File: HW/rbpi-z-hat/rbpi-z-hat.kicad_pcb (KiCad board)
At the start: 4 copper layers, 65 x 30 mm, 98 parts, among them IC1 BQ24315DSGR, J1 RBPI_CONN, J10 JST_GH, J11 Conn_01x10, J12 Conn_01x06, J13 Conn_01x10, J14 Conn_01x06, J15 Conn_01x06, J16 Conn_01x10, J8 Conn_01x06_MountingPin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

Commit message: Replaced LSM9DS1 with BMI160/QMI8658C
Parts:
- removed C23: 4.7uF/10V, Capacitor_SMD:C_0805_2012Metric
- removed C24, C25, C27: 0.1uF, Capacitor_SMD:C_0603_1608Metric
- removed C26: 10nF/16V, Capacitor_SMD:C_0603_1608Metric
- removed U8: LSM9DS1, Package_LGA:LGA-24L_3x3.5mm_P0.43mm
- added C16: 0.1uF, Capacitor_SMD:C_0603_1608Metric, F.Cu at (88.3, 65.7)
- added C35: 0.1uF, Capacitor_SMD:C_0603_1608Metric, F.Cu at (88.3, 68.2)
- added U10: BMI160, Package_LGA:Bosch_LGA-14_3x2.5mm_P0.5mm, F.Cu at (92.7, 66.6)
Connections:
- net /LSM_nCS renamed /BMI_nCS

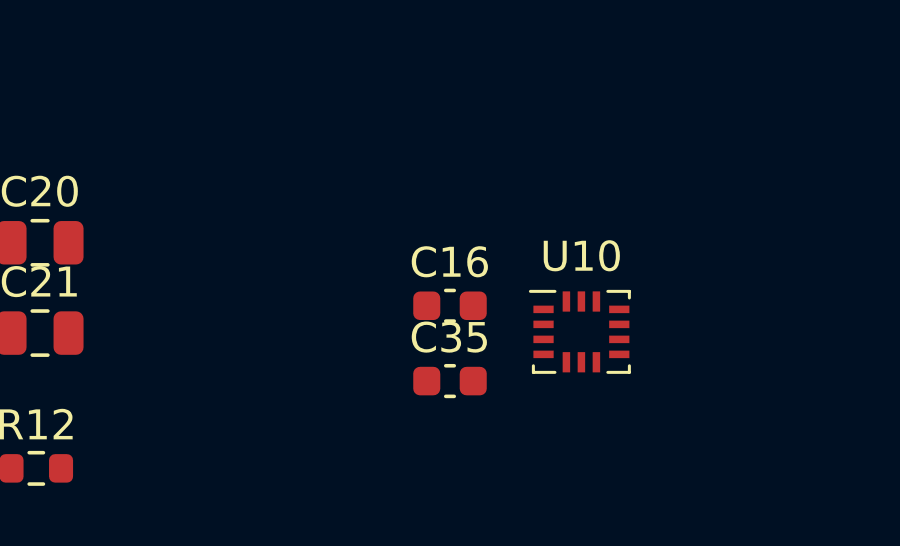
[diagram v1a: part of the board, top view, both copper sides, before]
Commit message: Changed capasitors to 0402
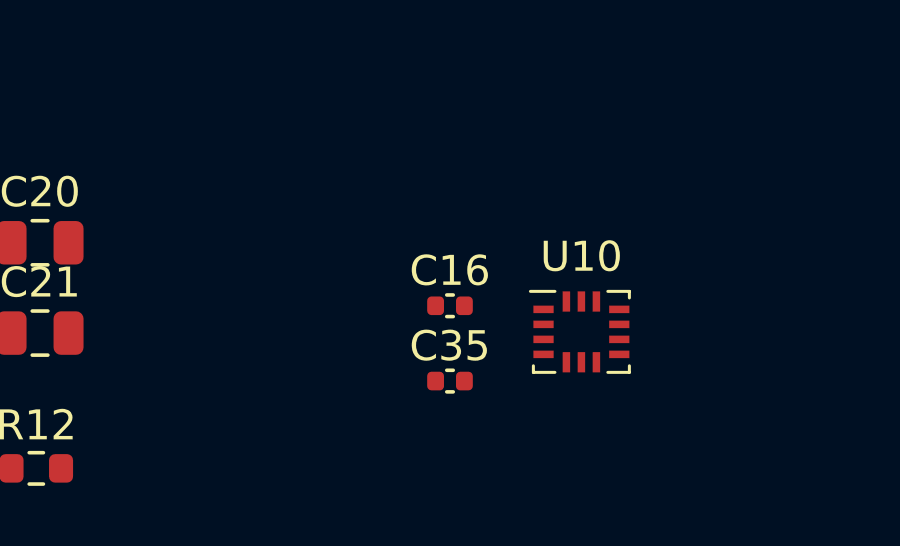
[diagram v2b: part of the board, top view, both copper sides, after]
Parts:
- C16, C35: footprint Capacitor_SMD:C_0603_1608Metric -> Capacitor_SMD:C_0402_1005Metric
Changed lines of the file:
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@@
     )
   )
-  (footprint "Capacitor_SMD:C_0603_1608Metric" (layer "F.Cu")
+  (footprint "Capacitor_SMD:C_0402_1005Metric" (layer "F.Cu")
     (at 88.275 68.21)
-    (descr "Capacitor SMD 0603 (1608 Metric), square (rectangular) end terminal, IPC_7351 nominal, (Body size source: IPC-SM-782 page 76, https://www.pcb-3d.com/wordpress/wp-content/uploads/ipc-sm-782a_amendment_1_and_2.pdf), generated with kicad-footprint-generator")
+    (descr "Capacitor SMD 0402 (1005 Metric), square (rectangular) end terminal, IPC_7351 nominal, (Body size source: IPC-SM-782 page 76, https://www.pcb-3d.com/wordpress/wp-content/uploads/ipc-sm-782a_amendment_1_and_2.pdf), generated with kicad-footprint-generator")
     (tags "capacitor")
     (property "Sheetfile" "BMI160_QMI8658C.kicad_sch")
@@
     (property "ki_keywords" "cap capacitor")
     (attr smd)
-    (fp_text reference "C35" (at 0 -1.43) (layer "F.SilkS")
-        (effects (font (size 1 1) (thickness 0.15)))
-    )
-    (fp_text value "0.1uF" (at 0 1.43) (layer "F.Fab")
+    (fp_text reference "C35" (at 0 -1.16) (layer "F.SilkS")
+        (effects (font (size 1 1) (thickness 0.15)))
+    )
+    (fp_text value "0.1uF" (at 0 1.16) (layer "F.Fab")
         (effects (font (size 1 1) (thickness 0.15)))
     )
     (fp_text user "${REFERENCE}" (at 0 0) (layer "F.Fab")
-        (effects (font (size 0.4 0.4) (thickness 0.06)))
-    )
-    (fp_line (start -0.14058 -0.51) (end 0.14058 -0.51)
-      (stroke (width 0.12) (type solid)) (layer "F.SilkS"))
-    (fp_line (start -0.14058 0.51) (end 0.14058 0.51)
-      (stroke (width 0.12) (type solid)) (layer "F.SilkS"))
-    (fp_line (start -1.48 -0.73) (end 1.48 -0.73)
-      (stroke (width 0.05) (type solid)) (layer "F.CrtYd"))
-    (fp_line (start -1.48 0.73) (end -1.48 -0.73)
-      (stroke (width 0.05) (type solid)) (layer "F.CrtYd"))
-    (fp_line (start 1.48 -0.73) (end 1.48 0.73)
-      (stroke (width 0.05) (type solid)) (layer "F.CrtYd"))
-    (fp_line (start 1.48 0.73) (end -1.48 0.73)
-      (stroke (width 0.05) (type solid)) (layer "F.CrtYd"))
-    (fp_line (start -0.8 -0.4) (end 0.8 -0.4)
-      (stroke (width 0.1) (type solid)) (layer "F.Fab"))
-    (fp_line (start -0.8 0.4) (end -0.8 -0.4)
-      (stroke (width 0.1) (type solid)) (layer "F.Fab"))
-    (fp_line (start 0.8 -0.4) (end 0.8 0.4)
-      (stroke (width 0.1) (type solid)) (layer "F.Fab"))
-    (fp_line (start 0.8 0.4) (end -0.8 0.4)
-      (stroke (width 0.1) (type solid)) (layer "F.Fab"))
-    (pad "1" smd roundrect (at -0.775 0) (size 0.9 0.95) (layers "F.Cu" "F.Paste" "F.Mask") (roundrect_rratio 0.25)
+        (effects (font (size 0.25 0.25) (thickness 0.04)))
+    )
+    (fp_line (start -0.107836 -0.36) (end 0.107836 -0.36)
+      (stroke (width 0.12) (type solid)) (layer "F.SilkS"))
+    (fp_line (start -0.107836 0.36) (end 0.107836 0.36)
+      (stroke (width 0.12) (type solid)) (layer "F.SilkS"))
+    (fp_line (start -0.91 -0.46) (end 0.91 -0.46)
+      (stroke (width 0.05) (type solid)) (layer "F.CrtYd"))
+    (fp_line (start -0.91 0.46) (end -0.91 -0.46)
+      (stroke (width 0.05) (type solid)) (layer "F.CrtYd"))
+    (fp_line (start 0.91 -0.46) (end 0.91 0.46)
+      (stroke (width 0.05) (type solid)) (layer "F.CrtYd"))
+    (fp_line (start 0.91 0.46) (end -0.91 0.46)
+      (stroke (width 0.05) (type solid)) (layer "F.CrtYd"))
+    (fp_line (start -0.5 -0.25) (end 0.5 -0.25)
+      (stroke (width 0.1) (type solid)) (layer "F.Fab"))
+    (fp_line (start -0.5 0.25) (end -0.5 -0.25)
+      (stroke (width 0.1) (type solid)) (layer "F.Fab"))
+    (fp_line (start 0.5 -0.25) (end 0.5 0.25)
+      (stroke (width 0.1) (type solid)) (layer "F.Fab"))
+    (fp_line (start 0.5 0.25) (end -0.5 0.25)
+      (stroke (width 0.1) (type solid)) (layer "F.Fab"))
+    (pad "1" smd roundrect (at -0.48 0) (size 0.56 0.62) (layers "F.Cu" "F.Paste" "F.Mask") (roundrect_rratio 0.25)
       (net 44 "/SENS_VDD") (pintype "passive"))
-    (pad "2" smd roundrect (at 0.775 0) (size 0.9 0.95) (layers "F.Cu" "F.Paste" "F.Mask") (roundrect_rratio 0.25)
+    (pad "2" smd roundrect (at 0.48 0) (size 0.56 0.62) (layers "F.Cu" "F.Paste" "F.Mask") (roundrect_rratio 0.25)
       (net 45 "/SENS_FGND") (pintype "passive"))
-    (model "${KICAD6_3DMODEL_DIR}/Capacitor_SMD.3dshapes/C_0603_1608Metric.wrl"
+    (model "${KICAD6_3DMODEL_DIR}/Capacitor_SMD.3dshapes/C_0402_1005Metric.wrl"
       (offset (xyz 0 0 0))
       (scale (xyz 1 1 1))
@@
       ))
   )
-  (footprint "Capacitor_SMD:C_0603_1608Metric" (layer "F.Cu")
+  (footprint "Capacitor_SMD:C_0402_1005Metric" (layer "F.Cu")
     (at 88.275 65.7)
-    (descr "Capacitor SMD 0603 (1608 Metric), square (rectangular) end terminal, IPC_7351 nominal, (Body size source: IPC-SM-782 page 76, https://www.pcb-3d.com/wordpress/wp-content/uploads/ipc-sm-782a_amendment_1_and_2.pdf), generated with kicad-footprint-generator")
+    (descr "Capacitor SMD 0402 (1005 Metric), square (rectangular) end terminal, IPC_7351 nominal, (Body size source: IPC-SM-782 page 76, https://www.pcb-3d.com/wordpress/wp-content/uploads/ipc-sm-782a_amendment_1_and_2.pdf), generated with kicad-footprint-generator")
     (tags "capacitor")
     (property "Sheetfile" "BMI160_QMI8658C.kicad_sch")
@@
     (property "ki_keywords" "cap capacitor")
     (attr smd)
-    (fp_text reference "C16" (at 0 -1.43) (layer "F.SilkS")
-        (effects (font (size 1 1) (thickness 0.15)))
-    )
-    (fp_text value "0.1uF" (at 0 1.43) (layer "F.Fab")
+    (fp_text reference "C16" (at 0 -1.16) (layer "F.SilkS")
+        (effects (font (size 1 1) (thickness 0.15)))
+    )
+    (fp_text value "0.1uF" (at 0 1.16) (layer "F.Fab")
         (effects (font (size 1 1) (thickness 0.15)))
     )
     (fp_text user "${REFERENCE}" (at 0 0) (layer "F.Fab")
-        (effects (font (size 0.4 0.4) (thickness 0.06)))
-    )
-    (fp_line (start -0.14058 -0.51) (end 0.14058 -0.51)
-      (stroke (width 0.12) (type solid)) (layer "F.SilkS"))
-    (fp_line (start -0.14058 0.51) (end 0.14058 0.51)
-      (stroke (width 0.12) (type solid)) (layer "F.SilkS"))
-    (fp_line (start -1.48 -0.73) (end 1.48 -0.73)
-      (stroke (width 0.05) (type solid)) (layer "F.CrtYd"))
-    (fp_line (start -1.48 0.73) (end -1.48 -0.73)
-      (stroke (width 0.05) (type solid)) (layer "F.CrtYd"))
-    (fp_line (start 1.48 -0.73) (end 1.48 0.73)
-      (stroke (width 0.05) (type solid)) (layer "F.CrtYd"))
-    (fp_line (start 1.48 0.73) (end -1.48 0.73)
-      (stroke (width 0.05) (type solid)) (layer "F.CrtYd"))
-    (fp_line (start -0.8 -0.4) (end 0.8 -0.4)
-      (stroke (width 0.1) (type solid)) (layer "F.Fab"))
-    (fp_line (start -0.8 0.4) (end -0.8 -0.4)
-      (stroke (width 0.1) (type solid)) (layer "F.Fab"))
-    (fp_line (start 0.8 -0.4) (end 0.8 0.4)
-      (stroke (width 0.1) (type solid)) (layer "F.Fab"))
-    (fp_line (start 0.8 0.4) (end -0.8 0.4)
-      (stroke (width 0.1) (type solid)) (layer "F.Fab"))
-    (pad "1" smd roundrect (at -0.775 0) (size 0.9 0.95) (layers "F.Cu" "F.Paste" "F.Mask") (roundrect_rratio 0.25)
+        (effects (font (size 0.25 0.25) (thickness 0.04)))
+    )
+    (fp_line (start -0.107836 -0.36) (end 0.107836 -0.36)
+      (stroke (width 0.12) (type solid)) (layer "F.SilkS"))
+    (fp_line (start -0.107836 0.36) (end 0.107836 0.36)
+      (stroke (width 0.12) (type solid)) (layer "F.SilkS"))
+    (fp_line (start -0.91 -0.46) (end 0.91 -0.46)
+      (stroke (width 0.05) (type solid)) (layer "F.CrtYd"))
+    (fp_line (start -0.91 0.46) (end -0.91 -0.46)
+      (stroke (width 0.05) (type solid)) (layer "F.CrtYd"))
+    (fp_line (start 0.91 -0.46) (end 0.91 0.46)
+      (stroke (width 0.05) (type solid)) (layer "F.CrtYd"))
+    (fp_line (start 0.91 0.46) (end -0.91 0.46)
+      (stroke (width 0.05) (type solid)) (layer "F.CrtYd"))
+    (fp_line (start -0.5 -0.25) (end 0.5 -0.25)
+      (stroke (width 0.1) (type solid)) (layer "F.Fab"))
+    (fp_line (start -0.5 0.25) (end -0.5 -0.25)
+      (stroke (width 0.1) (type solid)) (layer "F.Fab"))
+    (fp_line (start 0.5 -0.25) (end 0.5 0.25)
+      (stroke (width 0.1) (type solid)) (layer "F.Fab"))
+    (fp_line (start 0.5 0.25) (end -0.5 0.25)
+      (stroke (width 0.1) (type solid)) (layer "F.Fab"))
+    (pad "1" smd roundrect (at -0.48 0) (size 0.56 0.62) (layers "F.Cu" "F.Paste" "F.Mask") (roundrect_rratio 0.25)
       (net 44 "/SENS_VDD") (pintype "passive"))
-    (pad "2" smd roundrect (at 0.775 0) (size 0.9 0.95) (layers "F.Cu" "F.Paste" "F.Mask") (roundrect_rratio 0.25)
+    (pad "2" smd roundrect (at 0.48 0) (size 0.56 0.62) (layers "F.Cu" "F.Paste" "F.Mask") (roundrect_rratio 0.25)
       (net 45 "/SENS_FGND") (pintype "passive"))
-    (model "${KICAD6_3DMODEL_DIR}/Capacitor_SMD.3dshapes/C_0603_1608Metric.wrl"
-      (offset (xyz 0 0 0))
-      (scale (xyz 1 1 1))
+    (model "${KICAD6_3DMODEL_DIR}/Capacitor_SMD.3dshapes/C_0402_1005Metric.wrl"
+      (offset (xyz 0 0 0))
+      (scale (xyz 1 1 1))

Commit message: Changes in PCB
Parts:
- moved C15 7.25 mm to (94.9, 40.1)
- moved C35 7.23 mm to (95.5, 68.0), turned to -90 degrees
- moved C14 6.72 mm to (96.7, 42.9), turned to 90 degrees
- moved C16 5.44 mm to (92.6, 69.0)
- moved C10 4.80 mm to (86.9, 48.8), turned to 90 degrees
- moved C13 1.15 mm to (90.6, 42.5), turned to 180 degrees
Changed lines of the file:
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@@
   )
   (footprint "Capacitor_SMD:C_0402_1005Metric" (layer "F.Cu")
-    (at 90.01 43.48)
+    (at 96.7 42.9 90)
     (descr "Capacitor SMD 0402 (1005 Metric), square (rectangular) end terminal, IPC_7351 nominal, (Body size source: IPC-SM-782 page 76, https://www.pcb-3d.com/wordpress/wp-content/uploads/ipc-sm-782a_amendment_1_and_2.pdf), generated with kicad-footprint-generator")
     (tags "capacitor")
@@
     (property "ki_keywords" "cap capacitor")
     (attr smd)
-    (fp_text reference "C14" (at 0 -1.16) (layer "F.SilkS")
-        (effects (font (size 1 1) (thickness 0.15)))
-    )
-    (fp_text value "4.7uF" (at 0 1.16) (layer "F.Fab")
-        (effects (font (size 1 1) (thickness 0.15)))
-    )
-    (fp_text user "${REFERENCE}" (at 0 0) (layer "F.Fab")
+    (fp_text reference "C14" (at 0 1.3 90) (layer "F.SilkS")
+        (effects (font (size 1 1) (thickness 0.15)))
+    )
+    (fp_text value "4.7uF" (at 0 1.16 90) (layer "F.Fab")
+        (effects (font (size 1 1) (thickness 0.15)))
+    )
+    (fp_text user "${REFERENCE}" (at 0 0 90) (layer "F.Fab")
         (effects (font (size 0.25 0.25) (thickness 0.04)))
     )
@@
     (fp_line (start 0.5 0.25) (end -0.5 0.25)
       (stroke (width 0.1) (type solid)) (layer "F.Fab"))
-    (pad "1" smd roundrect (at -0.48 0) (size 0.56 0.62) (layers "F.Cu" "F.Paste" "F.Mask") (roundrect_rratio 0.25)
+    (pad "1" smd roundrect (at -0.48 0 90) (size 0.56 0.62) (layers "F.Cu" "F.Paste" "F.Mask") (roundrect_rratio 0.25)
       (net 132 "Net-(U6-CAP)") (pintype "passive"))
-    (pad "2" smd roundrect (at 0.48 0) (size 0.56 0.62) (layers "F.Cu" "F.Paste" "F.Mask") (roundrect_rratio 0.25)
+    (pad "2" smd roundrect (at 0.48 0 90) (size 0.56 0.62) (layers "F.Cu" "F.Paste" "F.Mask") (roundrect_rratio 0.25)
       (net 45 "/SENS_FGND") (pintype "passive"))
     (model "${KICAD6_3DMODEL_DIR}/Capacitor_SMD.3dshapes/C_0402_1005Metric.wrl"
@@
   )
   (footprint "Capacitor_SMD:C_0402_1005Metric" (layer "F.Cu")
-    (at 90.01 41.51)
+    (at 90.6 42.5 180)
     (descr "Capacitor SMD 0402 (1005 Metric), square (rectangular) end terminal, IPC_7351 nominal, (Body size source: IPC-SM-782 page 76, https://www.pcb-3d.com/wordpress/wp-content/uploads/ipc-sm-782a_amendment_1_and_2.pdf), generated with kicad-footprint-generator")
     (tags "capacitor")
@@
     (fp_line (start 0.5 0.25) (end -0.5 0.25)
       (stroke (width 0.1) (type solid)) (layer "F.Fab"))
-    (pad "1" smd roundrect (at -0.48 0) (size 0.56 0.62) (layers "F.Cu" "F.Paste" "F.Mask") (roundrect_rratio 0.25)
+    (pad "1" smd roundrect (at -0.48 0 180) (size 0.56 0.62) (layers "F.Cu" "F.Paste" "F.Mask") (roundrect_rratio 0.25)
       (net 44 "/SENS_VDD") (pintype "passive"))
-    (pad "2" smd roundrect (at 0.48 0) (size 0.56 0.62) (layers "F.Cu" "F.Paste" "F.Mask") (roundrect_rratio 0.25)
+    (pad "2" smd roundrect (at 0.48 0 180) (size 0.56 0.62) (layers "F.Cu" "F.Paste" "F.Mask") (roundrect_rratio 0.25)
       (net 131 "Net-(C13-Pad2)") (pintype "passive"))
     (model "${KICAD6_3DMODEL_DIR}/Capacitor_SMD.3dshapes/C_0402_1005Metric.wrl"
@@
   )
   (footprint "Capacitor_SMD:C_0402_1005Metric" (layer "F.Cu")
-    (at 90.01 45.45)
+    (at 94.9 40.1)
     (descr "Capacitor SMD 0402 (1005 Metric), square (rectangular) end terminal, IPC_7351 nominal, (Body size source: IPC-SM-782 page 76, https://www.pcb-3d.com/wordpress/wp-content/uploads/ipc-sm-782a_amendment_1_and_2.pdf), generated with kicad-footprint-generator")
     (tags "capacitor")
@@
     (property "ki_keywords" "cap capacitor")
     (attr smd)
-    (fp_text reference "C15" (at 0 -1.16) (layer "F.SilkS")
+    (fp_text reference "C15" (at 2.4 0) (layer "F.SilkS")
         (effects (font (size 1 1) (thickness 0.15)))
     )
@@
   )
   (footprint "Capacitor_SMD:C_0402_1005Metric" (layer "F.Cu")
-    (at 88.275 68.21)
+    (at 95.5 68 -90)
     (descr "Capacitor SMD 0402 (1005 Metric), square (rectangular) end terminal, IPC_7351 nominal, (Body size source: IPC-SM-782 page 76, https://www.pcb-3d.com/wordpress/wp-content/uploads/ipc-sm-782a_amendment_1_and_2.pdf), generated with kicad-footprint-generator")
     (tags "capacitor")
@@
     (property "ki_keywords" "cap capacitor")
     (attr smd)
-    (fp_text reference "C35" (at 0 -1.16) (layer "F.SilkS")
-        (effects (font (size 1 1) (thickness 0.15)))
-    )
-    (fp_text value "0.1uF" (at 0 1.16) (layer "F.Fab")
-        (effects (font (size 1 1) (thickness 0.15)))
-    )
-    (fp_text user "${REFERENCE}" (at 0 0) (layer "F.Fab")
+    (fp_text reference "C35" (at 0 -1.16 90) (layer "F.SilkS")
+        (effects (font (size 1 1) (thickness 0.15)))
+    )
+    (fp_text value "0.1uF" (at 0 1.16 90) (layer "F.Fab")
+        (effects (font (size 1 1) (thickness 0.15)))
+    )
+    (fp_text user "${REFERENCE}" (at 0 0 90) (layer "F.Fab")
         (effects (font (size 0.25 0.25) (thickness 0.04)))
     )
@@
     (fp_line (start 0.5 0.25) (end -0.5 0.25)
       (stroke (width 0.1) (type solid)) (layer "F.Fab"))
-    (pad "1" smd roundrect (at -0.48 0) (size 0.56 0.62) (layers "F.Cu" "F.Paste" "F.Mask") (roundrect_rratio 0.25)
+    (pad "1" smd roundrect (at -0.48 0 270) (size 0.56 0.62) (layers "F.Cu" "F.Paste" "F.Mask") (roundrect_rratio 0.25)
       (net 44 "/SENS_VDD") (pintype "passive"))
-    (pad "2" smd roundrect (at 0.48 0) (size 0.56 0.62) (layers "F.Cu" "F.Paste" "F.Mask") (roundrect_rratio 0.25)
+    (pad "2" smd roundrect (at 0.48 0 270) (size 0.56 0.62) (layers "F.Cu" "F.Paste" "F.Mask") (roundrect_rratio 0.25)
       (net 45 "/SENS_FGND") (pintype "passive"))
     (model "${KICAD6_3DMODEL_DIR}/Capacitor_SMD.3dshapes/C_0402_1005Metric.wrl"
@@
     (property "ki_keywords" "I2C magnetic 3-axis sensor")
     (attr smd)
-    (fp_text reference "U6" (at 0 -2.7) (layer "F.SilkS")
+    (fp_text reference "U6" (at -1.02 -2.6) (layer "F.SilkS")
         (effects (font (size 1 1) (thickness 0.15)))
     )
@@
   )
   (footprint "Capacitor_SMD:C_0402_1005Metric" (layer "F.Cu")
-    (at 83.46 45.45)
+    (at 86.9 48.8 90)
     (descr "Capacitor SMD 0402 (1005 Metric), square (rectangular) end terminal, IPC_7351 nominal, (Body size source: IPC-SM-782 page 76, https://www.pcb-3d.com/wordpress/wp-content/uploads/ipc-sm-782a_amendment_1_and_2.pdf), generated with kicad-footprint-generator")
     (tags "capacitor")
@@
     (property "ki_keywords" "cap capacitor")
     (attr smd)
-    (fp_text reference "C10" (at 0 -1.16) (layer "F.SilkS")
-        (effects (font (size 1 1) (thickness 0.15)))
-    )
-    (fp_text value "4.7uF" (at 0 1.16) (layer "F.Fab")
-        (effects (font (size 1 1) (thickness 0.15)))
-    )
-    (fp_text user "${REFERENCE}" (at 0 0) (layer "F.Fab")
+    (fp_text reference "C10" (at 0 1.2 90) (layer "F.SilkS")
+        (effects (font (size 1 1) (thickness 0.15)))
+    )
+    (fp_text value "4.7uF" (at 0 1.16 90) (layer "F.Fab")
+        (effects (font (size 1 1) (thickness 0.15)))
+    )
+    (fp_text user "${REFERENCE}" (at 0 0 90) (layer "F.Fab")
         (effects (font (size 0.25 0.25) (thickness 0.04)))
     )
@@
     (fp_line (start 0.5 0.25) (end -0.5 0.25)
       (stroke (width 0.1) (type solid)) (layer "F.Fab"))
-    (pad "1" smd roundrect (at -0.48 0) (size 0.56 0.62) (layers "F.Cu" "F.Paste" "F.Mask") (roundrect_rratio 0.25)
+    (pad "1" smd roundrect (at -0.48 0 90) (size 0.56 0.62) (layers "F.Cu" "F.Paste" "F.Mask") (roundrect_rratio 0.25)
       (net 130 "Net-(U3-C1)") (pintype "passive"))
-    (pad "2" smd roundrect (at 0.48 0) (size 0.56 0.62) (layers "F.Cu" "F.Paste" "F.Mask") (roundrect_rratio 0.25)
+    (pad "2" smd roundrect (at 0.48 0 90) (size 0.56 0.62) (layers "F.Cu" "F.Paste" "F.Mask") (roundrect_rratio 0.25)
       (net 45 "/SENS_FGND") (pintype "passive"))
     (model "${KICAD6_3DMODEL_DIR}/Capacitor_SMD.3dshapes/C_0402_1005Metric.wrl"
@@
   )
   (footprint "Capacitor_SMD:C_0402_1005Metric" (layer "F.Cu")
-    (at 88.275 65.7)
+    (at 92.6 69)
     (descr "Capacitor SMD 0402 (1005 Metric), square (rectangular) end terminal, IPC_7351 nominal, (Body size source: IPC-SM-782 page 76, https://www.pcb-3d.com/wordpress/wp-content/uploads/ipc-sm-782a_amendment_1_and_2.pdf), generated with kicad-footprint-generator")
     (tags "capacitor")
@@
     (property "ki_keywords" "cap capacitor")
     (attr smd)
-    (fp_text reference "C16" (at 0 -1.16) (layer "F.SilkS")
-        (effects (font (size 1 1) (thickness 0.15)))
-    )
+    (fp_text reference "C16" (at 0 1.3) (layer "F.SilkS")
+        (effects (font (size 1 1) (thickness 0.15)))
+    )

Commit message: Changes in Sch & PCB
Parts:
- C1, C2, C4, C9, JP1, U2, U5: moved to B.Cu
- C20, C21, C28: footprint Capacitor_SMD:C_0805_2012Metric -> Capacitor_SMD:C_0603_1608Metric
- C29, C30, C32, C33, C34: footprint Capacitor_SMD:C_0603_1608Metric -> Capacitor_SMD:C_0402_1005Metric
- C3: footprint Capacitor_SMD:C_1206_3216Metric -> Capacitor_SMD:C_0805_2012Metric
- L10: footprint Inductor_SMD:L_0805_2012Metric -> Inductor_SMD:L_0603_1608Metric
- L5, L6, L7, L8: footprint Inductor_SMD:L_0603_1608Metric -> Inductor_SMD:L_0402_1005Metric
- R12: footprint Resistor_SMD:R_0603_1608Metric -> Resistor_SMD:R_0402_1005Metric; moved to B.Cu
- moved C14 87.5 mm to (15.9, 9.30)
- moved U6 86.9 mm to (13.4, 9.60)
- moved C15 86.7 mm to (14.7, 7.20)
- moved C13 86.1 mm to (11.0, 9.80), turned to -90 degrees
- moved C16 82.2 mm to (28.6, 17.4)
- moved C35 82.2 mm to (31.5, 16.4)
- moved U10 82.2 mm to (28.7, 15.0)
- moved C10 74.7 mm to (23.3, 9.64)
- moved U3 74.7 mm to (20.7, 9.55)
- moved C7 74.0 mm to (17.8, 9.34), turned to 180 degrees
- moved C6 70.4 mm to (22.0, 7.14)
- moved JP3 67.2 mm to (20.5, 13.1), turned to 180 degrees
- moved JP1 65.5 mm to (20.5, 13.1), turned to 180 degrees
- moved C21 61.8 mm to (50.1, 9.90), turned to 90 degrees
- moved R12 60.8 mm to (50.8, 15.1)
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
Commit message: Update
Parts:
- added C23: 0.1uF, Capacitor_SMD:C_0402_1005Metric, F.Cu at (44.4, 15.9)
- added R4: 10K, Resistor_SMD:R_0402_1005Metric, F.Cu at (44.4, 17.0)
- added R5: 500K, Resistor_SMD:R_0402_1005Metric, F.Cu at (44.4, 18.1)
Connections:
- U7 pad 1: unconnected-(U7-BOOT0-Pad1) -> Net-(U7-BOOT0)
- U7 pad 10: /SDA1 -> /CH32V203G6U6/PWM_OUT6
- U7 pad 27: /CH32V203G6U6/PWM_OUT5 -> /SCL1
- U7 pad 28: /CH32V203G6U6/PWM_OUT6 -> /SDA1
- U7 pad 4: unconnected-(U7-NRST-Pad4) -> /CH32V203G6U6/CH32_nRST
- U7 pad 9: /SCL1 -> /CH32V203G6U6/PWM_OUT5
